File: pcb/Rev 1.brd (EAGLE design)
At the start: 76.8 x 76.8 mm, 256 parts, among them J1 3220-10-0100-00, J2 10118194-0001LF, J3 B2B-PH-K-S(LF)(SN), Q1 MMBT3904,215MMBT3904,215, Q10 MMBT3904,215MMBT3904,215, Q11 MMBT3904,215MMBT3904,215, Q12 MMBT3904,215MMBT3904,215, Q13 MMBT3904,215MMBT3904,215, Q14 MMBT3904,215MMBT3904,215, Q15 MMBT3904,215MMBT3904,215, Q16 TEFT4300, Q17 TEFT4300, Q18 TEFT4300, Q19 TEFT4300, Q2 MMBT3904,215MMBT3904,215, Q20 MMBT3904,215MMBT3904,215, Q21 MMBT3904,215MMBT3904,215, Q22 MMBT3904,215MMBT3904,215, Q23 MMBT3904,215MMBT3904,215, Q24 TEFT4300, Q25 TEFT4300, Q26 TEFT4300, Q27 TEFT4300, Q28 SI7157DP, Q29 SI7157DP, Q3 MMBT3904,215MMBT3904,215, Q30 MMBT3906, Q31 MMBT3906, Q32 SI7157DP, Q33 MMBT3906, Q34 MMBT3906, Q4 MMBT3904,215MMBT3904,215, Q5 MMBT3904,215MMBT3904,215, Q6 MMBT3904,215MMBT3904,215, Q7 MMBT3904,215MMBT3904,215, Q8 MMBT3904,215MMBT3904,215, Q9 MMBT3904,215MMBT3904,215, SW1 210-10MS, U1 ATSAMD21G18A-MU, U10 DRV8871, U2 AP3441, U3 TPS61089, U4 BNO055, U5 MCP73811, U7 DRV8871, U8 DRV8871, U9 DRV8871

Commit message: Sorted into groups
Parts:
- R15: value (none) -> 30R
- moved R67 645.2 mm to (448.3, 228.6)
- moved R68 645.2 mm to (444.5, 228.6)
- moved R69 645.2 mm to (440.7, 228.6)
- moved Q4 633.1 mm to (462.3, 124.5)
- moved Q13 623.9 mm to (447.0, 184.2)
- moved C26 621.2 mm to (463.6, 176.5)
- moved C27 621.2 mm to (459.7, 176.5)
- moved C28 621.2 mm to (455.9, 176.5)
- moved C29 621.2 mm to (452.1, 176.5)
- moved C30 621.2 mm to (448.3, 176.5)
- moved C31 621.2 mm to (444.5, 176.5)
- moved C32 621.2 mm to (440.7, 176.5)
- moved C33 621.2 mm to (436.9, 176.5)
- moved C34 621.2 mm to (433.1, 176.5)
- moved C35 621.2 mm to (429.3, 176.5)
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
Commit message: Did some layout
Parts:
- moved C26 482.1 mm to (-5.08, 63.5)
- moved R26 482.1 mm to (-5.08, 66.0)
- moved C33 470.9 mm to (-5.08, 14.0)
- moved C32 467.2 mm to (7.62, 1.27)
- moved C27 464.0 mm to (7.62, 72.4)
- moved R27 464.0 mm to (7.62, 74.9)
- moved Q12 463.9 mm to (2.54, 64.8)
- moved R30 463.6 mm to (-1.27, 66.0)
- moved R37 456.6 mm to (-5.08, 16.5)
- moved Q23 454.2 mm to (2.54, 15.2)
- moved R36 453.1 mm to (7.62, 3.81)
- moved Q22 450.9 mm to (15.2, 2.54)
- moved C34 448.8 mm to (-1.27, 63.5)
- moved Q13 445.7 mm to (15.2, 73.7)
- moved R31 445.4 mm to (11.4, 74.9)
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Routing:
- net +12V: track 0.00 -> 13.8 mm
- net +3V7: track 0.00 -> 13.3 mm
- net N$17: track 0.00 -> 13.1 mm
- net N$10: track 0.00 -> 11.5 mm
- net N$13: track 0.00 -> 5.03 mm
- net N$11: track 0.00 -> 3.80 mm, vias 0 -> 1
- net N$14: track 0.00 -> 3.17 mm, vias 0 -> 1
- net N$12: track 0.00 -> 3.12 mm
- net N$8: track 0.00 -> 2.68 mm, vias 0 -> 1
- net N$15: track 0.00 -> 1.91 mm
- net N$9: track 0.00 -> 1.88 mm

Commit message: Placed the majority of the components
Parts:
- C1, C10, C11, C12, C13, C14, C2, C20, C21, C23, C24, C3, C4, C5, C6, C63, C64, C79, C8, C9, FB1, FB2, FB3, R12, R13, R14, R48, R49, R52, R53, R54, R63, R9: device Micromouse 2020:0805 -> Micromouse 2020:0402
- C15, C33, C40, C52, C53, C54, C55, C56, C57, C7, C77, R1, R10, R11, R2, R42, R43, R44, R45, R46, R47, R5, R50, R51, R55, R56, R57, R67, R68, R69, R70, R71, R72, R73, R74, R75, R76, R77, R78, R79, R80, R81, R82, R83, R84, R85, R86: device Micromouse 2020:0805 -> Micromouse 2020:0603
- moved C45 501.0 mm to (-39.9, 81.5)
- moved C46 501.0 mm to (-43.7, 81.5)
- moved C47 501.0 mm to (-47.5, 81.5)
- moved C48 501.0 mm to (-51.3, 81.5)
- moved C49 501.0 mm to (-55.1, 81.5)
- moved C50 501.0 mm to (-58.9, 81.5)
- moved C51 501.0 mm to (-62.7, 81.5)
- moved D10 501.0 mm to (-62.7, 67.6)
- moved D2 501.0 mm to (-22.1, 67.6)
- moved D3 501.0 mm to (-27.2, 67.6)
- moved D5 501.0 mm to (-37.3, 67.6)
- moved D6 501.0 mm to (-42.4, 67.6)
- moved D7 501.0 mm to (-47.5, 67.6)
- moved D9 501.0 mm to (-57.7, 67.6)
- moved Q10 501.0 mm to (-58.9, 72.6)
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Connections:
- new net N$999: C63.2, C8.2, C9.2, FB2.1, FB3.1, U6.1
- net !RESET: now also C7.1, R1.1, R2.2; no longer C7.P$1, R1.P$1, R2.P$2
- net +12V: now also R14.2; no longer R14.P$2
- net +3V3: now also C15.2, C3.2, C33.2, C4.2, C40.2, C52.2, C53.2, C54.2, C6.2, C64.2, C7.2, C77.2, FB1.2, R1.2, R10.2, R43.2, R44.2, R5.2, R50.2, R51.2, R63.2, R77.2, R78.2, R79.2, R80.2, R81.2, R82.2, R83.2, R84.2, R85.2, R86.2; no longer C15.P$2, C3.P$2, C33.P$2, C4.P$2, C40.P$2, C52.P$2, C53.P$2, C54.P$2, C6.P$2, C64.P$2, C7.P$2, C77.P$2, FB1.P$2, R1.P$2, R10.P$2, R43.P$2, R44.P$2, R5.P$2, R50.P$2, R51.P$2, R63.P$2, R77.P$2, R78.P$2, R79.P$2, R80.P$2, R81.P$2, R82.P$2, R83.P$2, R84.P$2, R85.P$2, R86.P$2
- net +5V: now also R48.2, R49.2; no longer R48.P$2, R49.P$2
- net GND: now also C1.1, C10.1, C11.1, C12.1, C13.1, C14.1, C15.1, C2.1, C21.1, C23.1, C24.1, C3.1, C33.1, C4.1, C40.1, C5.1, C52.1, C53.1, C54.1, C55.1, C56.1, C57.1, C6.1, C63.1, C64.1, C77.1, C79.1, C8.1, C9.1, R11.1, R13.1, R42.1, R45.1, R46.1, R47.1, R52.1, R53.1, R54.1, R67.1, R68.1, R69.1, R70.1, R71.1, R72.1, R73.1, R74.1, R75.1, R76.1; no longer C1.P$1, C10.P$1, C11.P$1, C12.P$1, C13.P$1, C14.P$1, C15.P$1, C2.P$1, C21.P$1, C23.P$1, C24.P$1, C3.P$1, C33.P$1, C4.P$1, C40.P$1, C5.P$1, C52.P$1, C53.P$1, C54.P$1, C55.P$1, C56.P$1, C57.P$1, C6.P$1, C63.P$1, C64.P$1, C77.P$1, C79.P$1, C8.P$1, C9.P$1, R11.P$1, R13.P$1, R42.P$1, R45.P$1, R46.P$1, R47.P$1, R52.P$1, R53.P$1, R54.P$1, R67.P$1, R68.P$1, R69.P$1, R70.P$1, R71.P$1, R72.P$1, R73.P$1, R74.P$1, R75.P$1, R76.P$1
- net N$1: now also R2.1; no longer R2.P$1
- net N$10: now also C20.2, R9.2; no longer C20.P$2, R9.P$2
- net N$100: now also R73.2; no longer R73.P$2
- net N$101: now also R74.2; no longer R74.P$2
- net N$102: now also R75.2; no longer R75.P$2
- net N$103: now also R76.2; no longer R76.P$2
- net N$11: now also R11.2; no longer R11.P$2
- net N$12: now also C21.2; no longer C21.P$2
- net N$13: now also C23.2, R12.2; no longer C23.P$2, R12.P$2
- net N$14: now also R10.1; no longer R10.P$1
- net N$15: now also C24.2, R12.1; no longer C24.P$2, R12.P$1
- net N$17: now also R13.2, R14.1; no longer R13.P$2, R14.P$1
- net N$2: now also C5.2; no longer C5.P$2
- net N$4: now also C1.2, C2.2, FB1.1; no longer C1.P$2, C2.P$2, FB1.P$1
- net N$56: now also C55.2; no longer C55.P$2
- net N$57: now also R44.1; no longer R44.P$1
- net N$58: now also C56.2; no longer C56.P$2
- net N$59: now also R42.2; no longer R42.P$2
- net N$60: now also C57.2; no longer C57.P$2
- net N$61: now also R45.2; no longer R45.P$2
- net N$62: now also R43.1; no longer R43.P$1
- net N$63: now also R46.2; no longer R46.P$2
- net N$64: now also R47.2; no longer R47.P$2
- net N$66: now also R48.1; no longer R48.P$1
- net N$67: now also R49.1; no longer R49.P$1
- net N$68: now also R55.1; no longer R55.P$1
- net N$69: now also R55.2, R57.2; no longer R55.P$2, R57.P$2
- net N$70: now also R56.1; no longer R56.P$1
- net N$71: now also R56.2; no longer R56.P$2
- net N$72: now also R52.2; no longer R52.P$2
- net N$73: now also R53.2; no longer R53.P$2
- net N$74: now also R54.2; no longer R54.P$2
- net N$75: now also R57.1; no longer R57.P$1
- net N$8: now also C20.1; no longer C20.P$1
- net N$82: now also R63.1; no longer R63.P$1
- net N$9: now also R9.1; no longer R9.P$1
- net N$94: now also R67.2; no longer R67.P$2
- net N$95: now also R68.2; no longer R68.P$2
- net N$96: now also R69.2; no longer R69.P$2
- net N$97: now also R70.2; no longer R70.P$2
- net N$98: now also R71.2; no longer R71.P$2
- net N$99: now also R72.2; no longer R72.P$2
- net SCL: now also R50.1; no longer R50.P$1
- net SDA: now also R51.1; no longer R51.P$1
- net SW0: now also R86.1; no longer R86.P$1
- net SW1: now also R85.1; no longer R85.P$1
- net SW2: now also R84.1; no longer R84.P$1
- net SW3: now also R83.1; no longer R83.P$1
- net SW4: now also R82.1; no longer R82.P$1
- net SW5: now also R81.1; no longer R81.P$1
- net SW6: now also R80.1; no longer R80.P$1
- net SW7: now also R79.1; no longer R79.P$1
- net SW8: now also R78.1; no longer R78.P$1
- net SW9: now also R77.1; no longer R77.P$1
- net SWDCLK: now also R5.1; no longer R5.P$1
- net VREFA: now also C79.2, FB2.2; no longer C63.P$2, C79.P$2, C8.P$2, C9.P$2, FB2.P$1, FB2.P$2, FB3.P$1, U6.1
- net VREFB: now also C10.2, FB3.2; no longer C10.P$2, FB3.P$2
- net XIN: now also C13.2; no longer C13.P$2
- net XIN32: now also C11.2; no longer C11.P$2
- net XOUT: now also C14.2; no longer C14.P$2
- net XOUT32: now also C12.2; no longer C12.P$2
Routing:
- net +3V3: track 0.00 -> 467.2 mm
- net +3V7: track 13.3 -> 150.4 mm
- net +12V: track 13.8 -> 127.5 mm, vias 0 -> 3
- net +5V: track 0.00 -> 49.2 mm
- net N$69: track 0.00 -> 43.4 mm
- net SWDCLK: track 0.00 -> 28.2 mm, vias 0 -> 1
- net SWDIO: track 0.00 -> 27.3 mm, vias 0 -> 2
- net N$104: track 0.00 -> 18.5 mm
- net !RESET: track 0.00 -> 16.7 mm
- net N$65: track 0.00 -> 16.4 mm
- net N$6: track 0.00 -> 14.6 mm, vias 0 -> 1
- net N$17: track 13.1 -> 2.11 mm
- net N$75: track 0.00 -> 10.2 mm
- net N$89: track 0.00 -> 9.84 mm
- net N$80: track 0.00 -> 9.76 mm
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
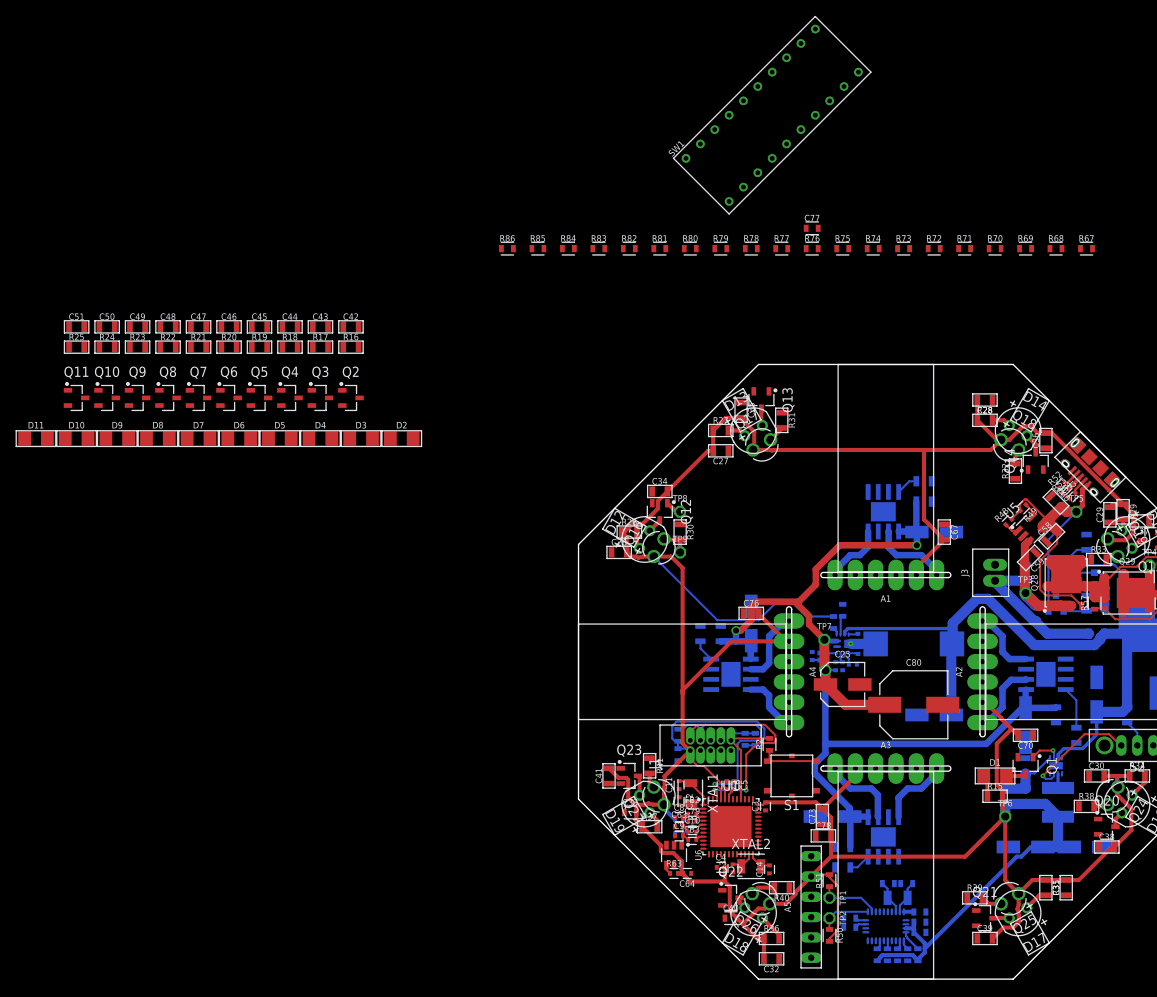
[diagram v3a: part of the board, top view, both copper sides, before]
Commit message: Placed the rest of the components
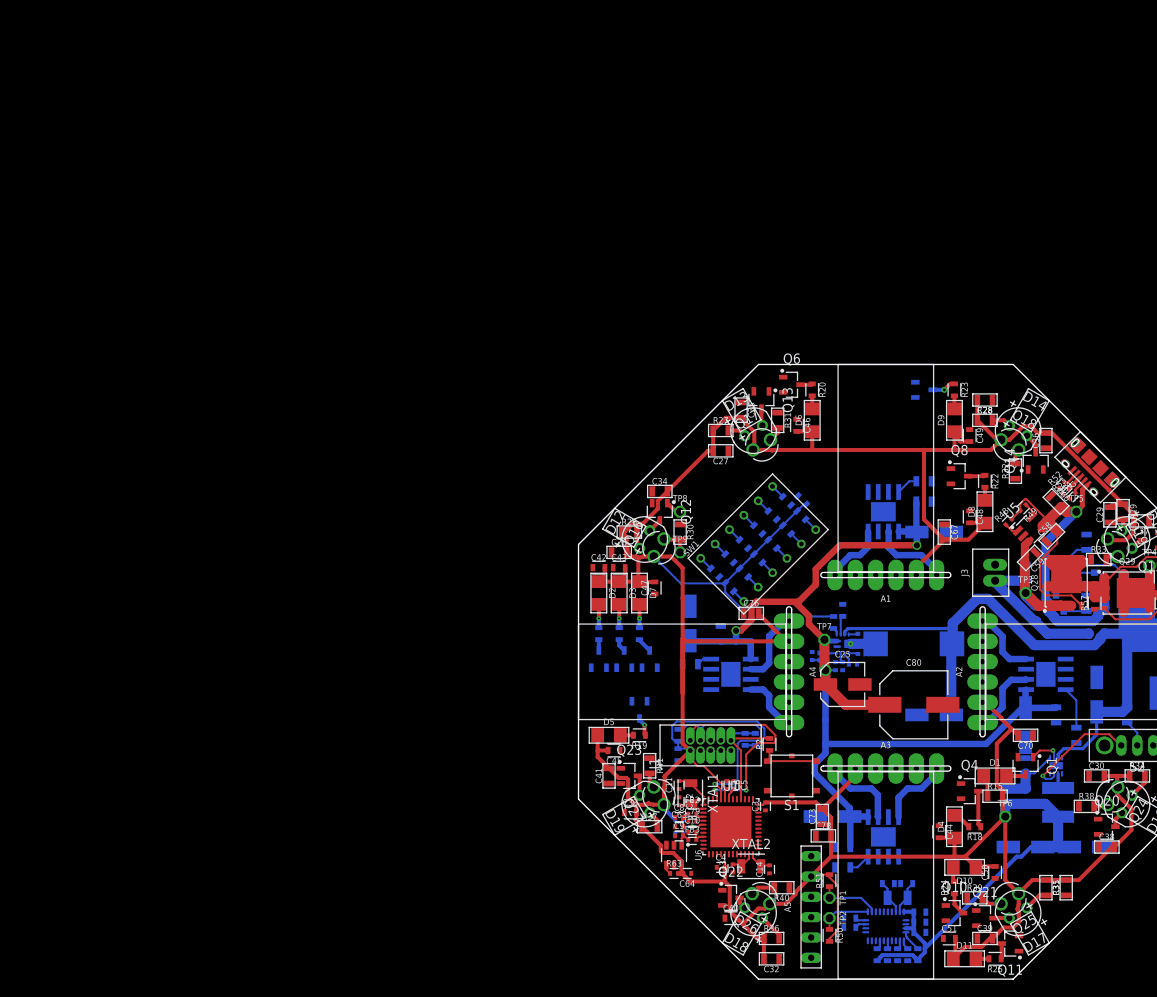
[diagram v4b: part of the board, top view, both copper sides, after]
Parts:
- removed R67, R68, R70: 10k, Micromouse 2020:0603
- removed R69: 10k\, Micromouse 2020:0603
- removed R77, R78, R79, R80: 470k, Micromouse 2020:0603
- C42, C43, C44, C45, C46, C47, C48, C49, C50, C51, R16, R17, R18, R19, R20, R21, R22, R23, R24, R25: device Micromouse 2020:0805 -> Micromouse 2020:0603
- SW1: value 210-10MS -> 210-6MS; device Micromouse 2020:210-10MS -> Micromouse 2020:210-6MS
- moved R25 137.9 mm to (52.1, 2.54), turned to 180 degrees
- moved Q11 135.2 mm to (54.0, 4.45), turned to 180 degrees
- moved C51 133.2 mm to (46.4, 5.08)
- moved D11 133.0 mm to (48.3, 2.54)
- moved C50 130.3 mm to (52.1, 13.3), turned to 90 degrees
- moved R24 125.6 mm to (47.0, 11.4), turned to 90 degrees
- moved Q10 124.0 mm to (47.0, 8.26)
- moved D10 123.3 mm to (48.3, 14.0), turned to 180 degrees
- moved C49 104.9 mm to (48.9, 67.9), turned to 270 degrees
- moved D9 104.7 mm to (47.0, 69.8), turned to 90 degrees
- moved R18 104.5 mm to (49.5, 19.1), turned to 180 degrees
- moved D8 103.8 mm to (50.8, 58.4), turned to 90 degrees
- moved R22 103.5 mm to (50.8, 62.2), turned to 270 degrees
- moved C48 103.0 mm to (48.9, 57.8), turned to 270 degrees
- moved C44 102.8 mm to (45.1, 18.4), turned to 270 degrees
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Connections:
- removed net N$94: R67.2, SW1.P11
- removed net N$95: R68.2, SW1.P12
- removed net N$96: R69.2, SW1.P13
- removed net N$97: R70.2, SW1.P14
- removed net SW6: R80.1, SW1.P7
- removed net SW7: R79.1, SW1.P8
- removed net SW8: R78.1, SW1.P9
- removed net SW9: R77.1, SW1.P10
- net +3V3: now also C42.2, C43.2, C44.2, C45.2, C46.2, C47.2, C48.2, C49.2, C50.2, C51.2, D10.1, D11.1, D2.1, D3.1, D4.1, D5.1, D6.1, D7.1, D8.1, D9.1; no longer C42.P$2, C43.P$2, C44.P$2, C45.P$2, C46.P$2, C47.P$2, C48.P$2, C49.P$2, C50.P$2, C51.P$2, R16.P$2, R17.P$2, R18.P$2, R19.P$2, R20.P$2, R21.P$2, R22.P$2, R23.P$2, R24.P$2, R25.P$2, R77.2, R78.2, R79.2, R80.2
- net GND: now also C42.1, C43.1, C44.1, C45.1, C46.1, C47.1, C48.1, C49.1, C50.1, C51.1; no longer C42.P$1, C43.P$1, C44.P$1, C45.P$1, C46.P$1, C47.P$1, C48.P$1, C49.P$1, C50.P$1, C51.P$1, R67.1, R68.1, R69.1, R70.1
- net N$100: now also SW1.P9; no longer SW1.P17
- net N$101: now also SW1.P10; no longer SW1.P18
- net N$102: now also SW1.P11; no longer SW1.P19
- net N$103: now also SW1.P12; no longer SW1.P20
- net N$20: now also R16.1; no longer D2.2
- net N$21: now also Q3.3, R17.1; no longer D2.1, R16.P$1
- net N$22: now also Q4.3, R18.1; no longer D3.2, Q3.3
- net N$23: now also Q5.3, R19.1; no longer D3.1, R17.P$1
- net N$24: now also Q6.3, R20.1; no longer D4.2, Q4.3
- net N$25: now also D2.2, R16.2; no longer D4.1, R18.P$1
- net N$26: now also D3.2, R17.2; no longer D5.2, Q5.3
- net N$27: now also D4.2, R18.2; no longer D5.1, R19.P$1
- net N$28: now also D5.2, R19.2; no longer D6.2, Q6.3
- net N$29: now also D6.2, R20.2; no longer D6.1, R20.P$1
- net N$30: now also R21.1; no longer D7.2
- net N$31: now also Q8.3, R22.1; no longer D7.1, R21.P$1
- net N$32: now also Q9.3, R23.1; no longer D8.2, Q8.3
- net N$33: now also Q10.3, R24.1; no longer D8.1, R22.P$1
- net N$34: now also Q11.3, R25.1; no longer D9.2, Q9.3
- net N$35: now also D7.2, R21.2; no longer D9.1, R23.P$1
- net N$36: now also D8.2, R22.2; no longer D10.2, Q10.3
- net N$37: now also D9.2, R23.2; no longer D10.1, R24.P$1
- net N$38: now also D10.2, R24.2; no longer D11.2, Q11.3
- net N$39: now also D11.2, R25.2; no longer D11.1, R25.P$1
- net N$98: now also SW1.P7; no longer SW1.P15
- net N$99: now also SW1.P8; no longer SW1.P16
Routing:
- net +3V3: track 467.2 -> 540.2 mm
- net +5V: track 49.2 -> 57.9 mm
- net N$22: track 0.00 -> 4.57 mm
- net +12V: track 127.5 -> 131.2 mm
- net N$32: track 0.00 -> 3.04 mm, vias 0 -> 1
- net N$35: track 0.00 -> 2.91 mm, vias 0 -> 1
- net N$26: track 0.00 -> 2.91 mm, vias 0 -> 1
- net N$25: track 0.00 -> 2.91 mm, vias 0 -> 1
- net N$33: track 0.00 -> 2.87 mm
- net N$10: track 3.11 -> 5.89 mm
- net N$23: track 0.00 -> 2.41 mm, vias 0 -> 1
- net N$27: track 0.00 -> 2.38 mm
- net N$31: track 0.00 -> 2.14 mm
- net N$34: track 0.00 -> 1.94 mm
- net N$30: track 0.00 -> 1.87 mm
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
